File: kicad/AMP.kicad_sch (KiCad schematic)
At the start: 32 parts

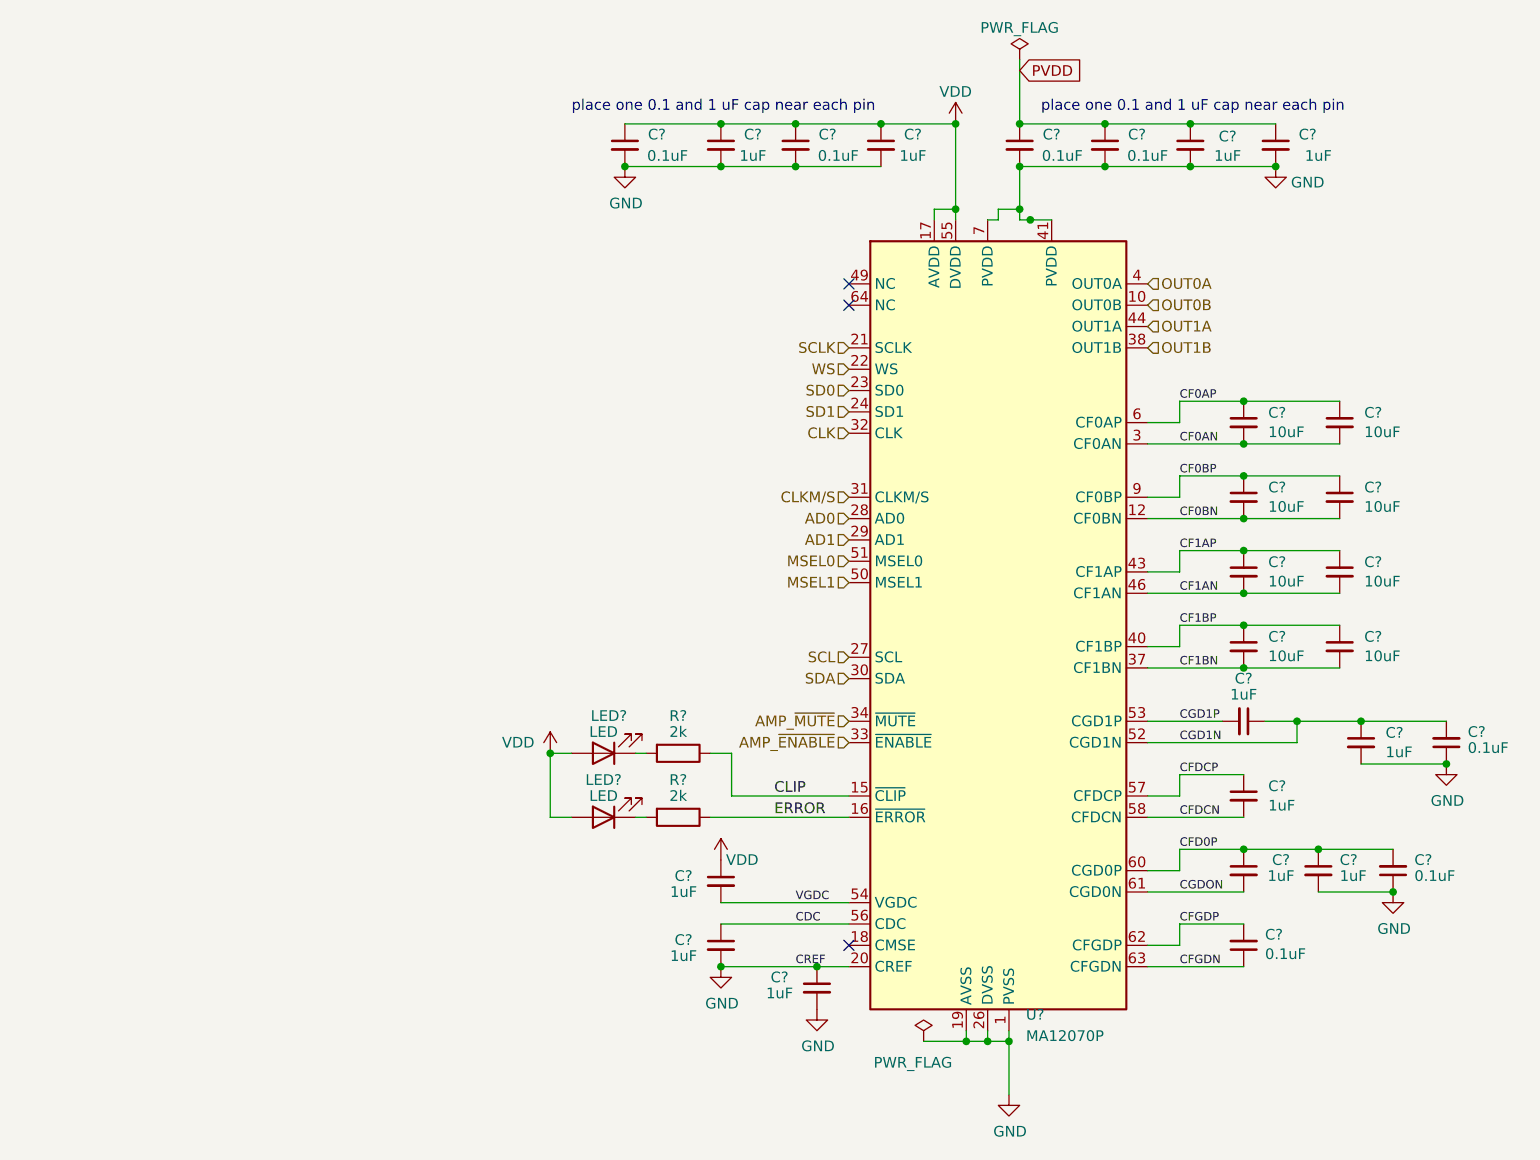
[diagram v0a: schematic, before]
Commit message: changed schematic layout
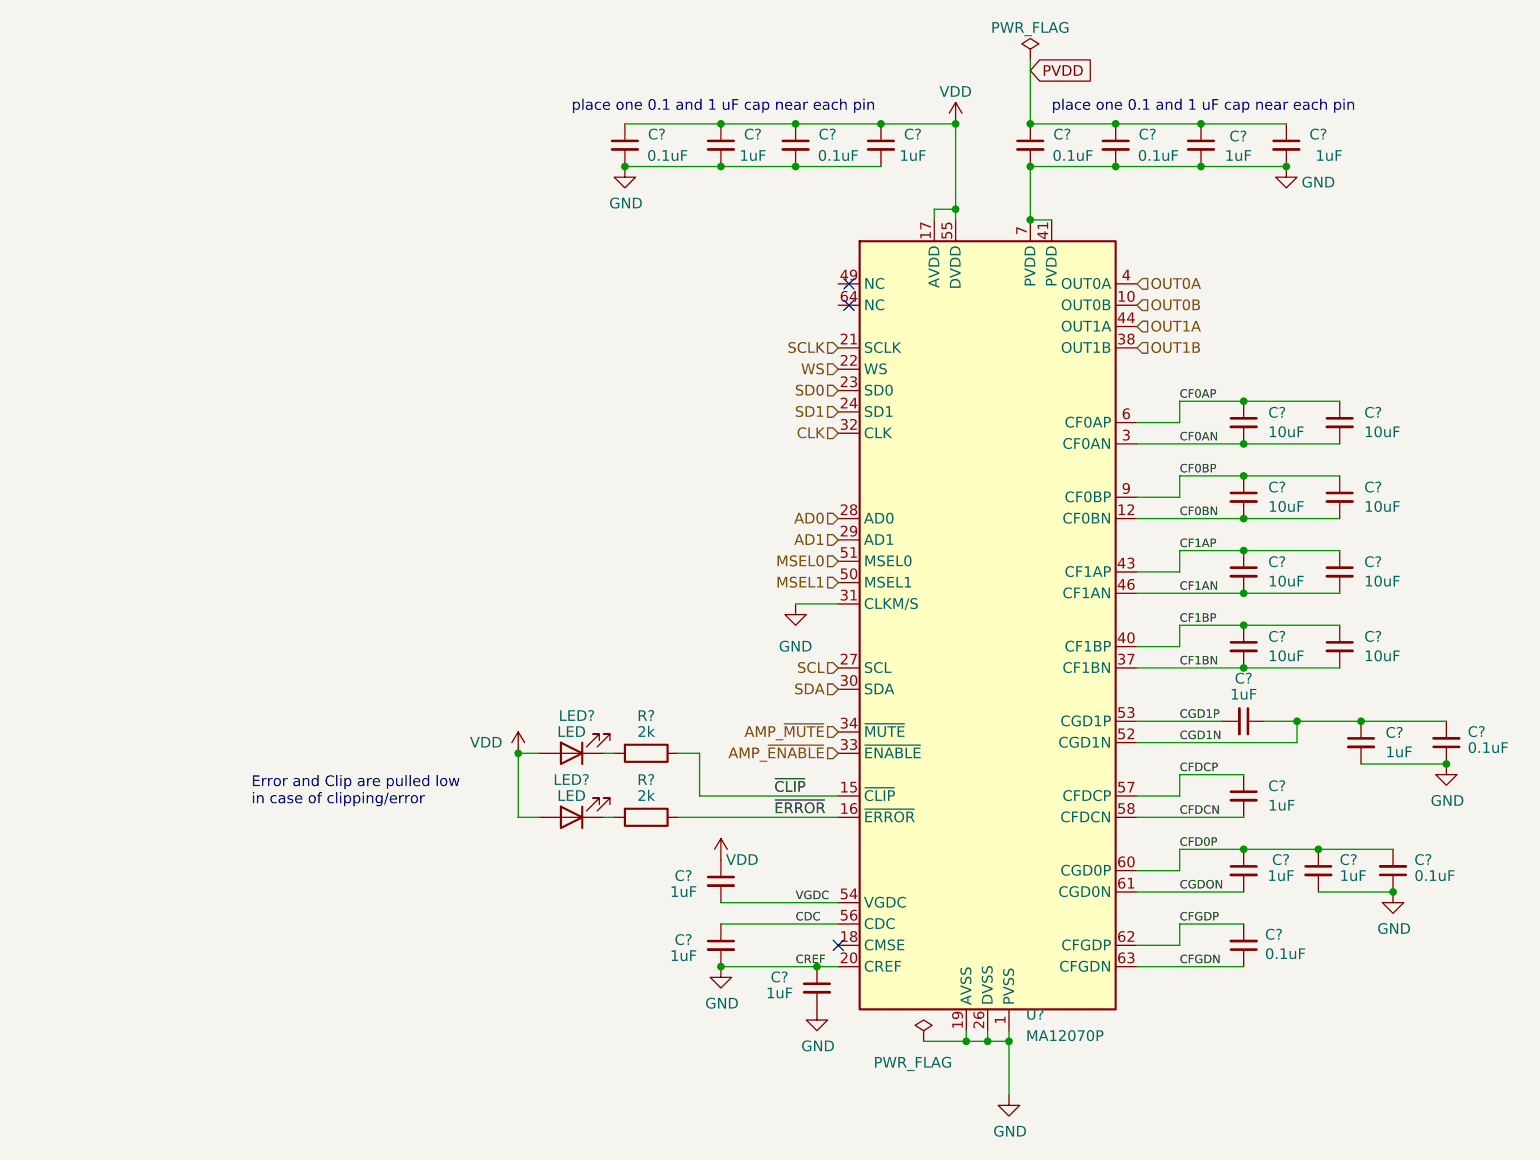
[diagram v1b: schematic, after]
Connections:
- net CLKM/S is gone; now on net GND: U?.31 (CLKM/S)
- net GND: now also U?.8 (PVDD)
- net CLIP renamed ~{CLIP}
- net ERROR renamed ~{ERROR}
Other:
- note added: "Error and Clip are pulled low in case of clipping/error"
- moved on the sheet: C?, LED?, R?, U?

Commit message: ongoing work
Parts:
- removed R?: 2k, Resistor_SMD:R_1206_3216Metric, symbol Device:R
- added C? (x4): 1uF, Capacitor_SMD:C_1206_3216Metric, symbol Device:C_Small
- added R?: 2k, Resistor_SMD:R_1206_3216Metric, symbol Device:R_Small
- R?: symbol Device:R -> Device:R_Small
- U?: symbol project_symbols:MA12070P -> project_symbols:MA12070
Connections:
- net MSEL0 is gone; now on net VDD: U?.51 (MSEL0)
- net MSEL1 is gone; now on net GND: U?.50 (MSEL1)
- net AMP_~{ENABLE}: now also U?.34 (~{MUTE}); no longer U?.33 (~{ENABLE})
- net AMP_~{MUTE}: now also U?.33 (~{ENABLE}); no longer U?.34 (~{MUTE})
- net GND: no longer U?.31 (CLKM/S)
- net VDD: now also U?.31 (CLKM/S)
- net ~{ERROR}: now also R?.1
- net at LED?.1 (K): now also R?.2
- net SCLK: no longer names the net of U?.21 (IN0A)
- net SCLK: now also C?.2
- net SD0: no longer names the net of U?.23 (IN1A)
- net SD0: now also C?.1
- net SD1: no longer names the net of U?.24 (IN1B)
- net SD1: now also C?.2
- net WS: no longer names the net of U?.22 (IN0B)
- net WS: now also C?.2
- new net IN0A: C?.1
- new net IN0B: C?.1
- new net IN1A: C?.2
- new net IN1B: C?.1
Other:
- note added: "Notes for Pin Config: * CLKM/S - pulled HIGH for CLK master mode * CMSE - Floationg = BLE config * AD0 and AD1 are used to configute the I2C adress * MSEL0 = 1 and MSEL1 = 0 for BTL 2 Channel Mode"
- moved on the sheet: C?, LED?, R?, U?
